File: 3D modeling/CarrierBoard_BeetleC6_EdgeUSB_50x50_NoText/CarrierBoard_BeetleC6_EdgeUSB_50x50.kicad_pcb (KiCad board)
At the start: 2 copper layers, 50 x 50 mm, 14 parts

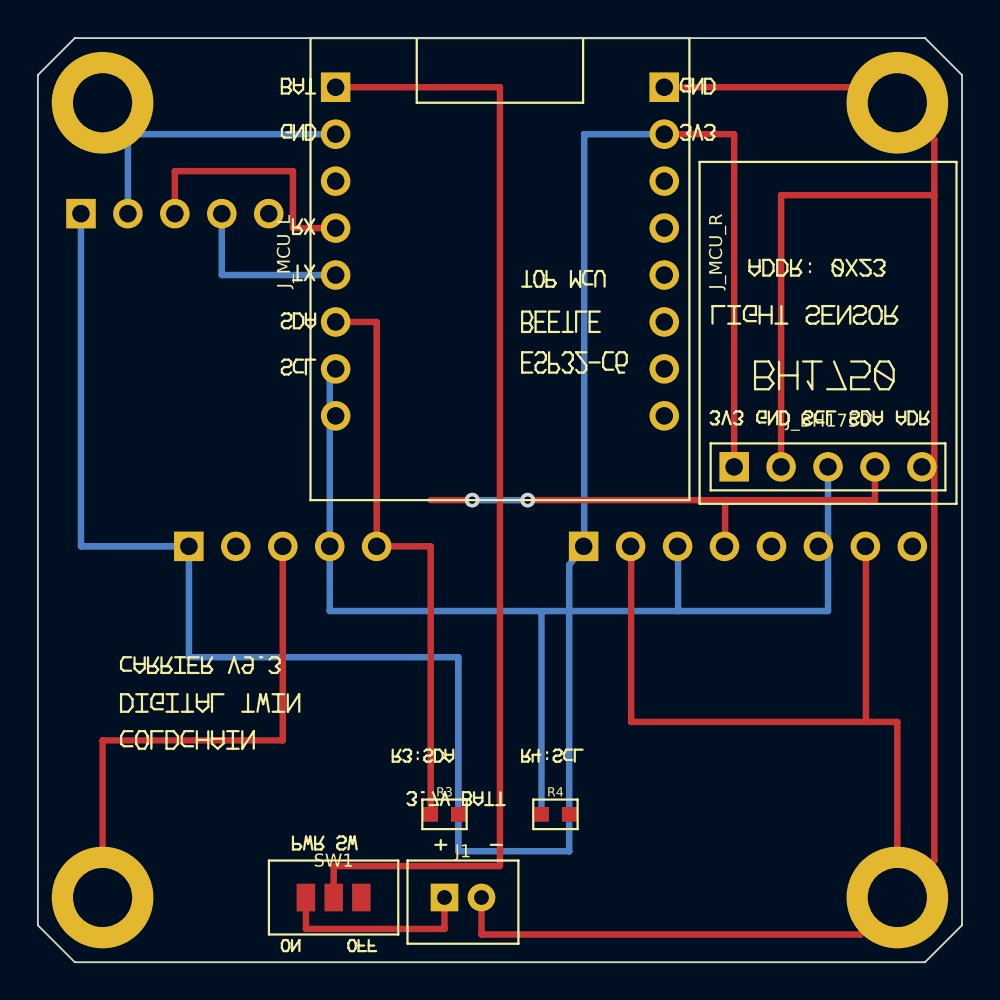
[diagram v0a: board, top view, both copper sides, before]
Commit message: feat(pcb): finalize 50x50 Carrier Board PCB routing, Gerber, STEP, BOM/CPL, and production deliverables
- Achieved KiCad 10.0 DRC 0 Errors & 0 Unconnected items
- Verified real-world pinouts: Beetle ESP32-C6, SHT45, BH1750, MPU6050, ATGM336H GPS
- Generated certified Gerber package (Gerber_CarrierBoard_BeetleC6_EdgeUSB_50x50_NoText.zip)
- Updated JLCPCB and DeviceMart compatible BOM and CPL files with exact coordinates
- Added 3D PCB renders and routing verification diagrams
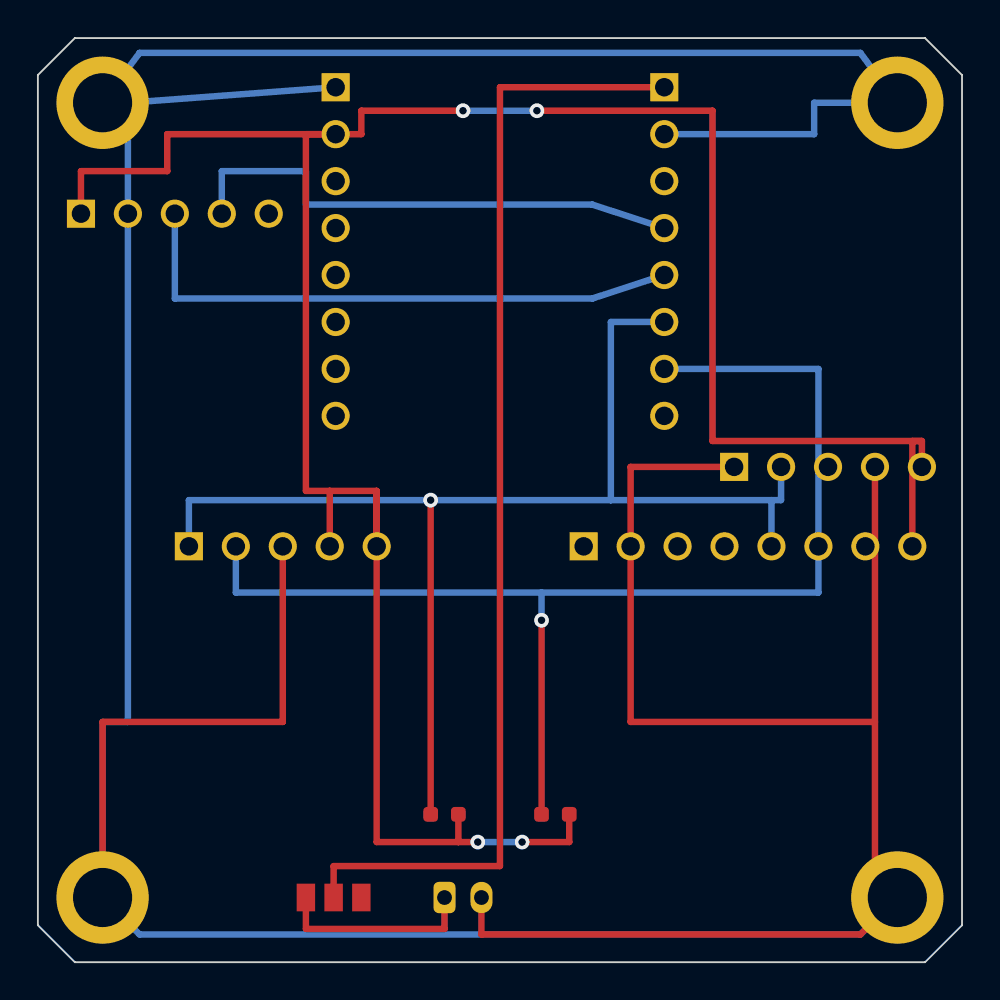
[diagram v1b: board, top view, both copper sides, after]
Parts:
- J_GPS, J_GY521, J_SHT45: moved to F.Cu
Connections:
- J_BH1750 pad 1: 3V3 -> GND
- J_BH1750 pad 2: GND -> I2C_SDA
- J_BH1750 pad 4: I2C_SDA -> GND
- J_BH1750 pad 5: GND -> 3V3
- J_GPS pad 3: GPS_RX -> GPS_TX
- J_GPS pad 4: GPS_TX -> GPS_RX
- J_GY521 pad 1: 3V3 -> (no net)
- J_GY521 pad 3: I2C_SCL -> (no net)
- J_GY521 pad 4: I2C_SDA -> (no net)
- J_GY521 pad 5: (no net) -> I2C_SDA
- J_GY521 pad 6: (no net) -> I2C_SCL
- J_GY521 pad 8: (no net) -> 3V3
- J_MCU_L pad 1: BAT -> GND
- J_MCU_L pad 2: GND -> 3V3
- J_MCU_L pad 4: GPS_RX -> (no net)
- J_MCU_L pad 5: GPS_TX -> (no net)
- J_MCU_L pad 6: I2C_SDA -> (no net)
- J_MCU_L pad 7: I2C_SCL -> (no net)
- J_MCU_R pad 1: GND -> BAT
- J_MCU_R pad 2: 3V3 -> GND
- J_MCU_R pad 4: (no net) -> GPS_RX
- J_MCU_R pad 5: (no net) -> GPS_TX
- J_MCU_R pad 6: (no net) -> I2C_SDA
- J_MCU_R pad 7: (no net) -> I2C_SCL
- J_SHT45 pad 1: 3V3 -> I2C_SDA
- J_SHT45 pad 2: (no net) -> I2C_SCL
- J_SHT45 pad 4: I2C_SCL -> 3V3
- J_SHT45 pad 5: I2C_SDA -> 3V3
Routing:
- net GND: track 196.6 -> 272.6 mm
- net GPS_TX: track 9.48 -> 31.3 mm
- net GPS_RX: track 14.1 -> 28.3 mm
- net 3V3: track 126.1 -> 139.7 mm, vias 0 -> 4
- net I2C_SDA: track 60.1 -> 68.4 mm, vias 2 -> 1
- net I2C_SCL: track 62.7 -> 67.0 mm, vias 0 -> 1
